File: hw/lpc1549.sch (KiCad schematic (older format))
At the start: 15 parts, among them J301 ARM_JTAG_SWD_HEADER_10_PINSMD, U301 MCP2551_SOIC8, U302 LPC1549JBD64, X301 XTAL_7A-12.000MAAJ-T

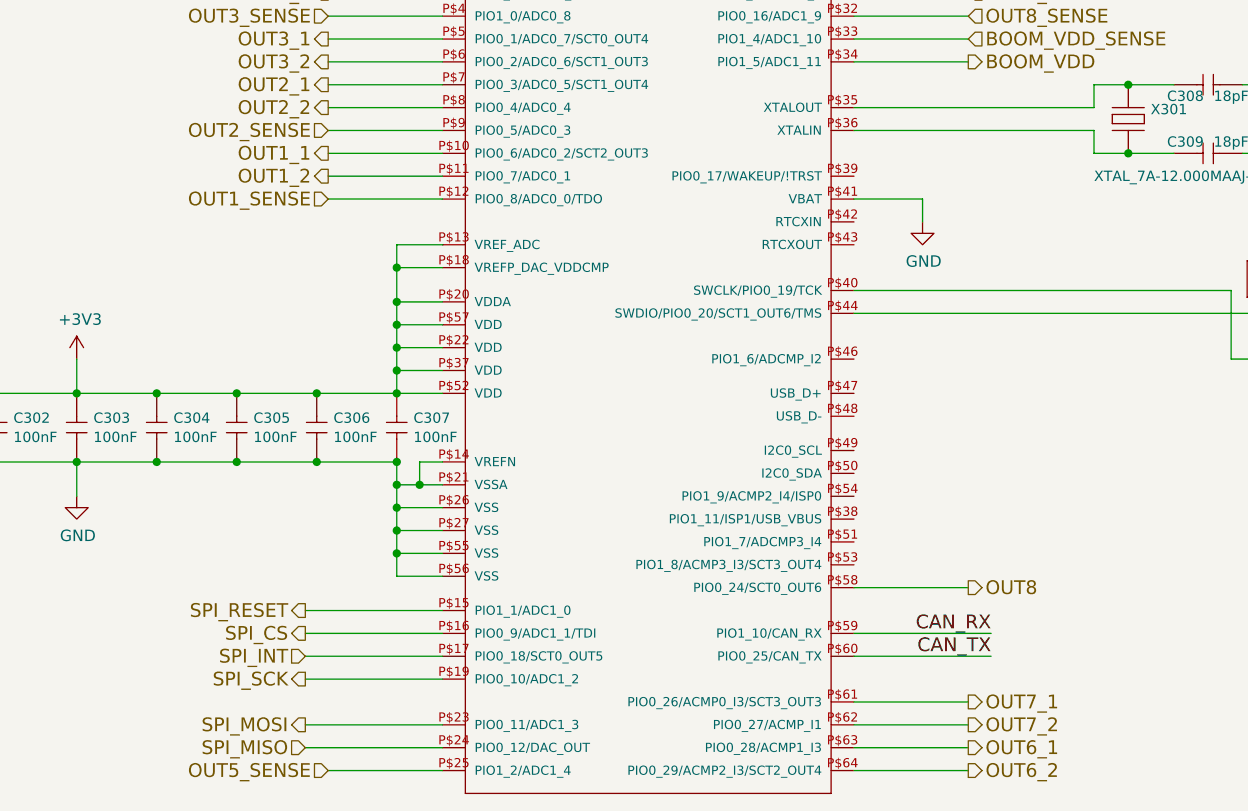
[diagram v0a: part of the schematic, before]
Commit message: hw 1.5.0, 2 ain inputs added
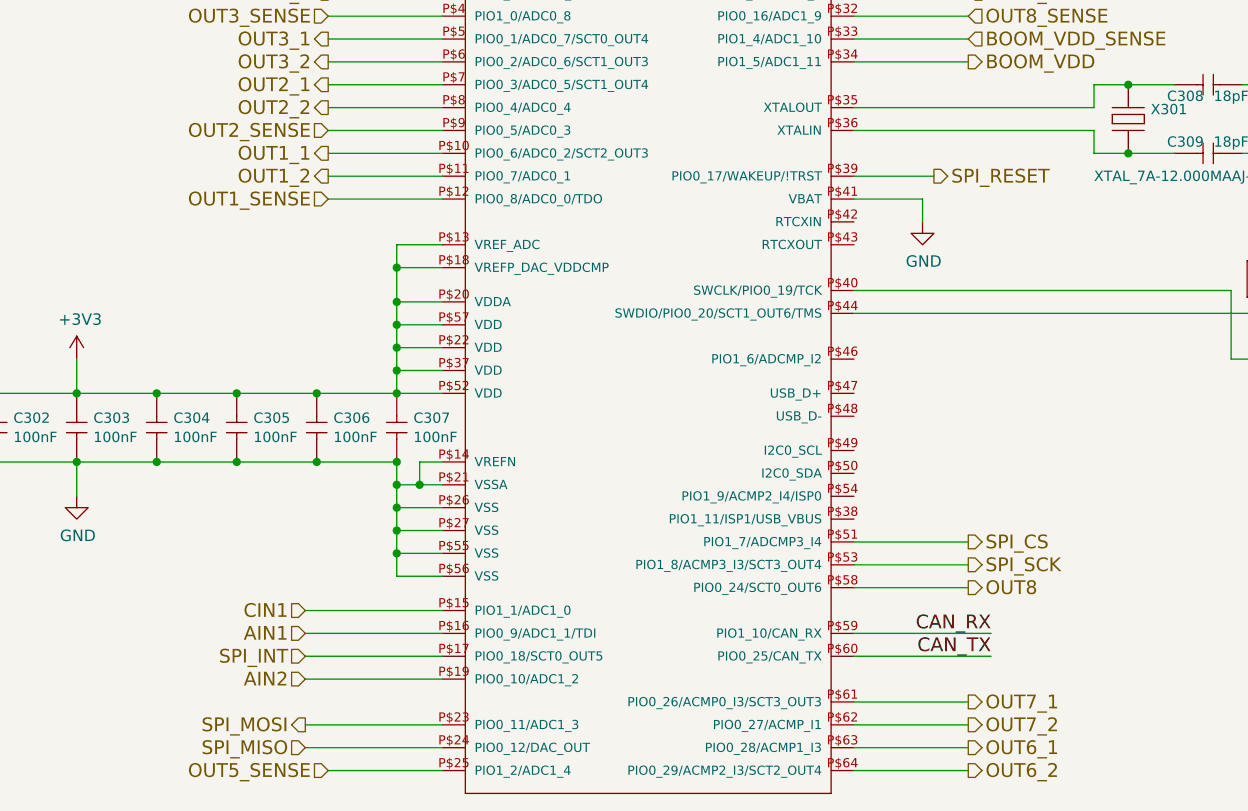
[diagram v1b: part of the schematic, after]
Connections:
- net SPI_CS: now also U302.P$51 (PIO1_7/ADCMP3_I4); no longer U302.P$16 (PIO0_9/ADC1_1/TDI)
- net SPI_RESET: now also U302.P$39 (PIO0_17/WAKEUP/!TRST); no longer U302.P$15 (PIO1_1/ADC1_0)
- net SPI_SCK: now also U302.P$53 (PIO1_8/ACMP3_I3/SCT3_OUT4); no longer U302.P$19 (PIO0_10/ADC1_2)
- new net AIN1: U302.P$16 (PIO0_9/ADC1_1/TDI)
- new net AIN2: U302.P$19 (PIO0_10/ADC1_2)
- new net CIN1: U302.P$15 (PIO1_1/ADC1_0)
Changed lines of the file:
@@
 $Descr A4 11693 8268
 encoding utf-8
-Sheet 3 13
+Sheet 3 14
 Title ""
 Date ""
@@
 	3600 4100 3950 4100
 Wire Wire Line
-	5200 5150 4600 5150
-Wire Wire Line
-	5200 5350 4600 5350
+	7000 4750 7500 4750
+Wire Wire Line
+	7000 4850 7500 4850
 Wire Wire Line
 	4600 5550 5200 5550
@@
 Text HLabel 4600 5550 0    60   Output ~ 0
 SPI_MOSI
-Text HLabel 4600 5350 0    60   Output ~ 0
+Text HLabel 7500 4850 2    60   Output ~ 0
 SPI_SCK
-Text HLabel 4600 5150 0    60   Output ~ 0
+Text HLabel 7500 4750 2    60   Output ~ 0
 SPI_CS
 Wire Wire Line
-	5200 5050 4600 5050
-Text HLabel 4600 5050 0    60   Output ~ 0
+	7000 3150 7350 3150
+Text HLabel 7350 3150 2    60   Output ~ 0
 SPI_RESET
 Wire Wire Line
@@
 Text HLabel 7500 2350 2    60   Input ~ 0
 OUT7_SENSE
+Wire Wire Line
+	5200 5350 4600 5350
+Wire Wire Line
+	5200 5150 4600 5150
+Wire Wire Line
+	4600 5050 5200 5050
+Text HLabel 4600 5050 0    60   Input ~ 0
+CIN1
+Text HLabel 4600 5150 0    60   Input ~ 0
+AIN1
+Text HLabel 4600 5350 0    60   Input ~ 0
+AIN2
 $EndSCHEMATC
